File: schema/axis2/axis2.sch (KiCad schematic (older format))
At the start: 18 parts, among them J1 JA, J2 JB, J3 5VPower, J4 12VPower, J5 Power Motor 1, J6 Power Motor 2, J7 M1, J8 M2, J9 RC-PPM, Q1 BC547, U1 gy-9250, U2 L7805, U3 axis2-frame

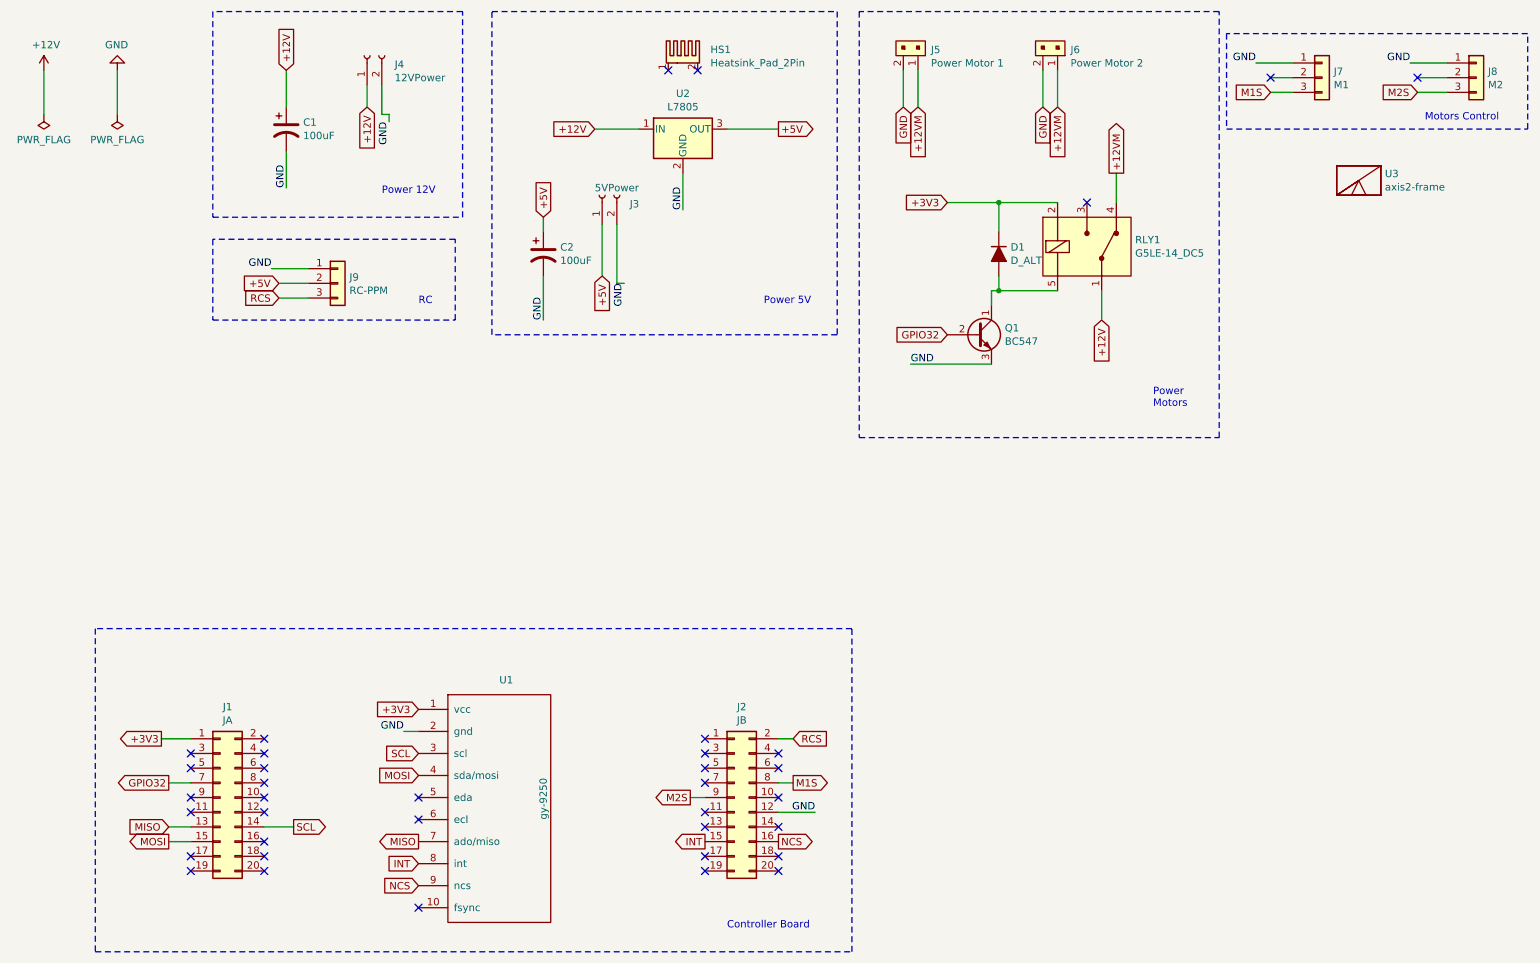
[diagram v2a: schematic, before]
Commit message: Corretto scheda per errato posizionamento alimentazione esp32
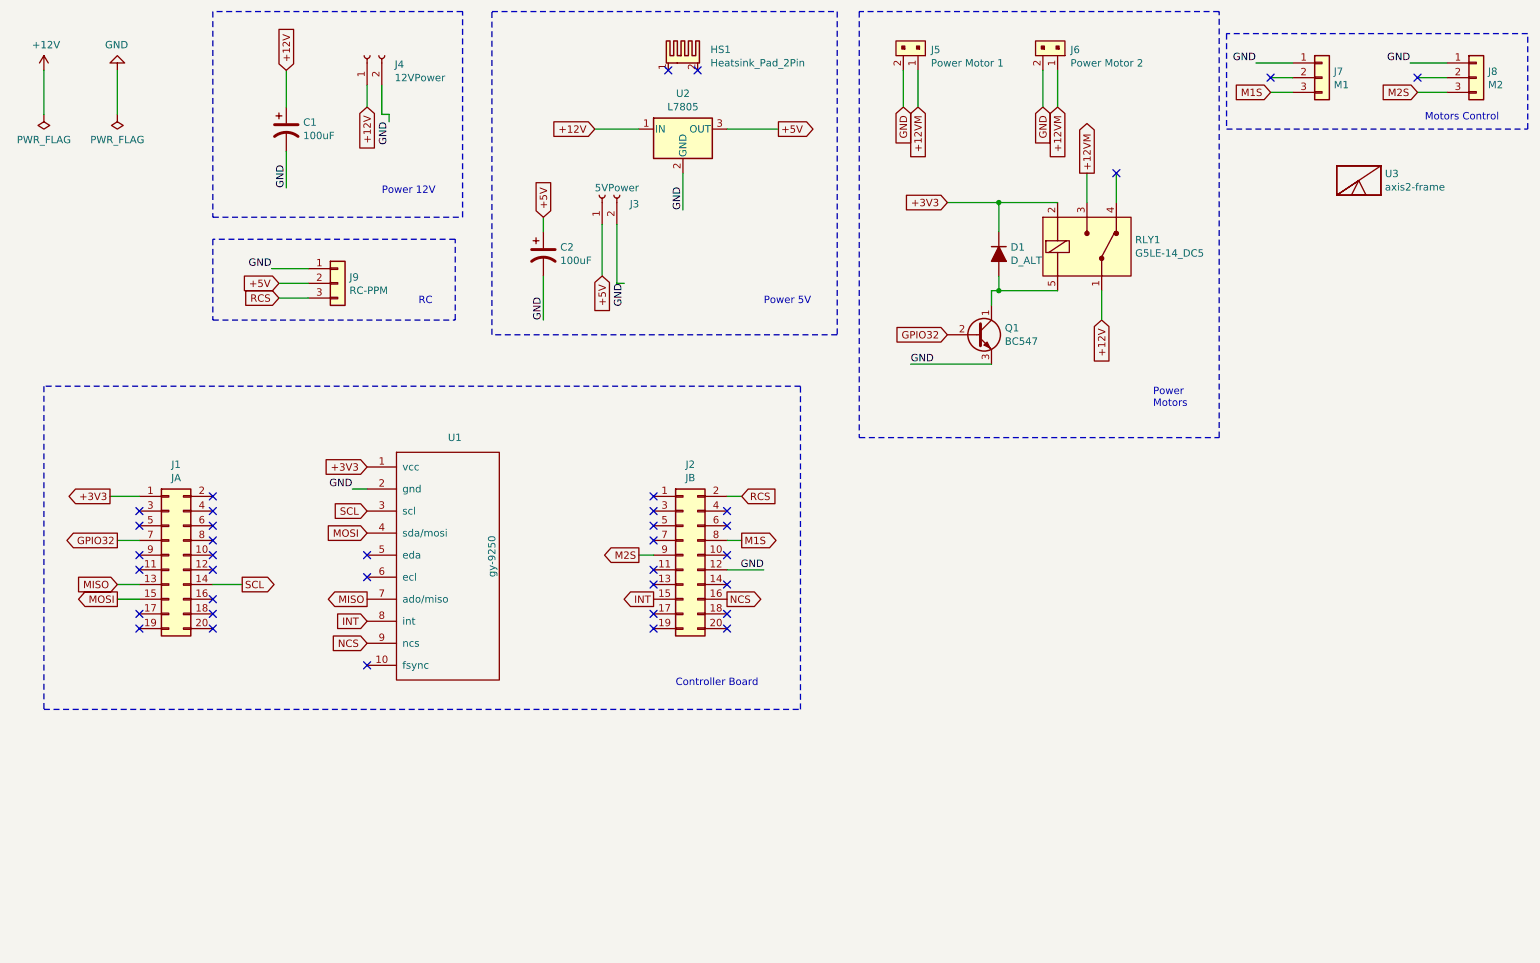
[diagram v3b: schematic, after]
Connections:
- net +12VM: now also RLY1.3 (NO); no longer RLY1.4 (NC)
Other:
- moved on the sheet: J1, J2, U1
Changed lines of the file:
@@
 L axis2-rescue:Conn_02x10_Odd_Even-Connector_Generic J1
 U 1 1 6072B308
-P 2250 6050
-F 0 "J1" H 2300 6667 50  0000 C CNN
-F 1 "JA" H 2300 6576 50  0000 C CNN
-F 2 "Connector_PinSocket_2.54mm:PinSocket_2x10_P2.54mm_Vertical" H 2250 6050 50  0001 C CNN
-F 3 "~" H 2250 6050 50  0001 C CNN
-	1    2250 6050
+P 1900 4400
+F 0 "J1" H 1950 5017 50  0000 C CNN
+F 1 "JA" H 1950 4926 50  0000 C CNN
+F 2 "Connector_PinSocket_2.54mm:PinSocket_2x10_P2.54mm_Vertical" H 1900 4400 50  0001 C CNN
+F 3 "~" H 1900 4400 50  0001 C CNN
+	1    1900 4400
 	1    0    0    -1
 $EndComp
@@
 L axis2-rescue:Conn_02x10_Odd_Even-Connector_Generic J2
 U 1 1 6072B4E0
-P 5750 6050
-F 0 "J2" H 5800 6667 50  0000 C CNN
-F 1 "JB" H 5800 6576 50  0000 C CNN
-F 2 "Connector_PinSocket_2.54mm:PinSocket_2x10_P2.54mm_Vertical" H 5750 6050 50  0001 C CNN
-F 3 "~" H 5750 6050 50  0001 C CNN
-	1    5750 6050
-	1    0    0    -1
-$EndComp
-NoConn ~ 2050 5750
-NoConn ~ 2050 5850
-NoConn ~ 2050 6050
-NoConn ~ 2050 6150
-NoConn ~ 2050 6450
-NoConn ~ 2050 6550
-NoConn ~ 2550 6550
-NoConn ~ 2550 6450
-NoConn ~ 2550 6350
-NoConn ~ 2550 6150
-NoConn ~ 2550 6050
-NoConn ~ 2550 5950
-NoConn ~ 2550 5850
-NoConn ~ 2550 5750
-NoConn ~ 2550 5650
-NoConn ~ 5550 5650
-NoConn ~ 5550 5750
-NoConn ~ 5550 5850
-NoConn ~ 5550 5950
-NoConn ~ 5550 6150
-NoConn ~ 5550 6250
-NoConn ~ 5550 6450
-NoConn ~ 5550 6550
-NoConn ~ 6050 6550
-NoConn ~ 6050 6450
+P 5400 4400
+F 0 "J2" H 5450 5017 50  0000 C CNN
+F 1 "JB" H 5450 4926 50  0000 C CNN
+F 2 "Connector_PinSocket_2.54mm:PinSocket_2x10_P2.54mm_Vertical" H 5400 4400 50  0001 C CNN
+F 3 "~" H 5400 4400 50  0001 C CNN
+	1    5400 4400
+	1    0    0    -1
+$EndComp
+NoConn ~ 1700 4100
+NoConn ~ 1700 4200
+NoConn ~ 1700 4400
+NoConn ~ 1700 4500
+NoConn ~ 1700 4800
+NoConn ~ 1700 4900
+NoConn ~ 2200 4900
+NoConn ~ 2200 4800
+NoConn ~ 2200 4700
+NoConn ~ 2200 4500
+NoConn ~ 2200 4400
+NoConn ~ 2200 4300
+NoConn ~ 2200 4200
+NoConn ~ 2200 4100
+NoConn ~ 2200 4000
+NoConn ~ 5200 4000
+NoConn ~ 5200 4100
+NoConn ~ 5200 4200
+NoConn ~ 5200 4300
+NoConn ~ 5200 4500
+NoConn ~ 5200 4600
+NoConn ~ 5200 4800
+NoConn ~ 5200 4900
+NoConn ~ 5700 4900
+NoConn ~ 5700 4800
 $Comp
 L gy-9250:gy-9250 U1
 U 1 1 6073C1B2
-P 4150 6150
-F 0 "U1" H 4150 7050 50  0000 L CNN
-F 1 "gy-9250" V 4450 6100 50  0000 L CNN
-F 2 "gy-9250_footprint:gy-9250" H 4150 6400 50  0001 C CNN
-F 3 "" H 4150 6400 50  0001 C CNN
-	1    4150 6150
-	1    0    0    -1
-$EndComp
-Wire Wire Line
-	1900 6250 2050 6250
-Text GLabel 3600 6350 0    50   Output ~ 0
+P 3800 4500
+F 0 "U1" H 3800 5400 50  0000 L CNN
+F 1 "gy-9250" V 4100 4450 50  0000 L CNN
+F 2 "gy-9250_footprint:gy-9250" H 3800 4750 50  0001 C CNN
+F 3 "" H 3800 4750 50  0001 C CNN
+	1    3800 4500
+	1    0    0    -1
+$EndComp
+Wire Wire Line
+	1550 4600 1700 4600
+Text GLabel 3250 4700 0    50   Output ~ 0
 MISO
-Text GLabel 1900 6250 0    50   Input ~ 0
+Text GLabel 1550 4600 0    50   Input ~ 0
 MISO
 Wire Wire Line
-	1900 6350 2050 6350
-Text GLabel 3600 5900 0    50   Input ~ 0
+	1550 4700 1700 4700
+Text GLabel 3250 4250 0    50   Input ~ 0
 MOSI
-Text GLabel 2750 6250 2    50   Output ~ 0
+Text GLabel 2400 4600 2    50   Output ~ 0
 SCL
 Wire Wire Line
-	2550 6250 2750 6250
-Text GLabel 1900 6350 0    50   Output ~ 0
+	2200 4600 2400 4600
+Text GLabel 1550 4700 0    50   Output ~ 0
 MOSI
-Text GLabel 1850 5650 0    50   Output ~ 0
+Text GLabel 1500 4000 0    50   Output ~ 0
 +3V3
 Wire Wire Line
-	1850 5650 2050 5650
-Text GLabel 3600 5450 0    50   Input ~ 0
+	1500 4000 1700 4000
+Text GLabel 3250 3800 0    50   Input ~ 0
 +3V3
-Text GLabel 6050 6350 2    50   Output ~ 0
+Text GLabel 5700 4700 2    50   Output ~ 0
 NCS
-Text GLabel 3600 6650 0    50   Input ~ 0
+Text GLabel 3250 5000 0    50   Input ~ 0
 NCS
-NoConn ~ 6050 6250
-NoConn ~ 6050 6050
-NoConn ~ 6050 5850
-NoConn ~ 6050 5750
-Text GLabel 5550 6350 0    50   Output ~ 0
+NoConn ~ 5700 4600
+NoConn ~ 5700 4400
+NoConn ~ 5700 4200
+NoConn ~ 5700 4100
+Text GLabel 5200 4700 0    50   Output ~ 0
 INT
-Text GLabel 3600 6500 0    50   Input ~ 0
+Text GLabel 3250 4850 0    50   Input ~ 0
 INT
-Text GLabel 3600 5750 0    50   Input ~ 0
+Text GLabel 3250 4100 0    50   Input ~ 0
 SCL
-NoConn ~ 3600 6800
-NoConn ~ 3600 6050
-NoConn ~ 3600 6200
+NoConn ~ 3250 5150
+NoConn ~ 3250 4400
+NoConn ~ 3250 4550
 $Comp
 L axis2-rescue:L7805-Regulator_Linear U2
@@
 Wire Wire Line
 	5400 1800 5400 2050
-Text Label 3500 5600 2    50   ~ 0
-GND
-Wire Wire Line
-	3600 5600 3500 5600
-Text Label 6300 6150 2    50   ~ 0
-GND
-Wire Wire Line
-	6050 6150 6300 6150
+Text Label 3150 3950 2    50   ~ 0
+GND
+Wire Wire Line
+	3250 3950 3150 3950
+Text Label 5950 4500 2    50   ~ 0
+GND
+Wire Wire Line
+	5700 4500 5950 4500
 Text Label 3400 1450 3    50   ~ 0
 GND
@@
 Power 5V
 Wire Notes Line
-	1400 7100 6550 7100
-Wire Notes Line
-	6550 7100 6550 4900
-Wire Notes Line
-	6550 4900 1400 4900
-Wire Notes Line
-	1400 4900 1400 7100
-Text Notes 5700 6950 0    50   ~ 0
+	1050 5450 6200 5450
+Wire Notes Line
+	6200 5450 6200 3250
+Wire Notes Line
+	6200 3250 1050 3250
+Wire Notes Line
+	1050 3250 1050 5450
+Text Notes 5350 5300 0    50   ~ 0
 Controller Board
 $Comp
@@
 Wire Wire Line
 	10400 1150 10600 1150
-Text GLabel 6150 5950 2    50   Output ~ 0
+Text GLabel 5800 4300 2    50   Output ~ 0
 M1S
 Wire Wire Line
-	6050 5950 6150 5950
+	5700 4300 5800 4300
 Text GLabel 9400 1250 0    50   Input ~ 0
 M1S
@@
 Wire Wire Line
 	10400 1250 10600 1250
-Text GLabel 5450 6050 0    50   Output ~ 0
+Text GLabel 5100 4400 0    50   Output ~ 0
 M2S
 Wire Wire Line
-	5550 6050 5450 6050
+	5200 4400 5100 4400
 Wire Wire Line
 	4850 2150 4850 2500
@@
 Wire Wire Line
 	4950 2150 4950 2550
-Text GLabel 6150 5650 2    50   Input ~ 0
+Text GLabel 5800 4000 2    50   Input ~ 0
 RCS
 Wire Wire Line
-	6150 5650 6050 5650
+	5800 4000 5700 4000
 Text GLabel 2650 2650 0    50   Input ~ 0
 RCS
@@
 Wire Wire Line
 	8250 2800 8250 2600
-Text GLabel 8350 1800 1    50   Output ~ 0
+Text GLabel 8150 1800 1    50   Output ~ 0
 +12VM
 Wire Wire Line
 	8350 2000 8350 1800
-NoConn ~ 8150 2000
-Text GLabel 1900 5950 0    50   Output ~ 0
+NoConn ~ 8350 1800
+Text GLabel 1550 4300 0    50   Output ~ 0
 GPIO32
 Wire Wire Line
-	2050 5950 1900 5950
+	1700 4300 1550 4300
 $Comp
 L Device:D_ALT D1
@@
 Wire Wire Line
 	7500 3100 6950 3100
+Wire Wire Line
+	8150 2000 8150 1800
 $EndSCHEMATC
